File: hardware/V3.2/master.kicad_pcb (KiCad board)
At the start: 4 copper layers, 40 x 40 mm, 129 parts, among them J1 USB-C, J2 DRILL, J3 DRILL, J4 DRILL, J5 DRILL, J6 STACK-UP-HIGH, J7 STACK-HIGH, J8 STACK-UP-LOW, J9 STACK-DOWN, P1 Port A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

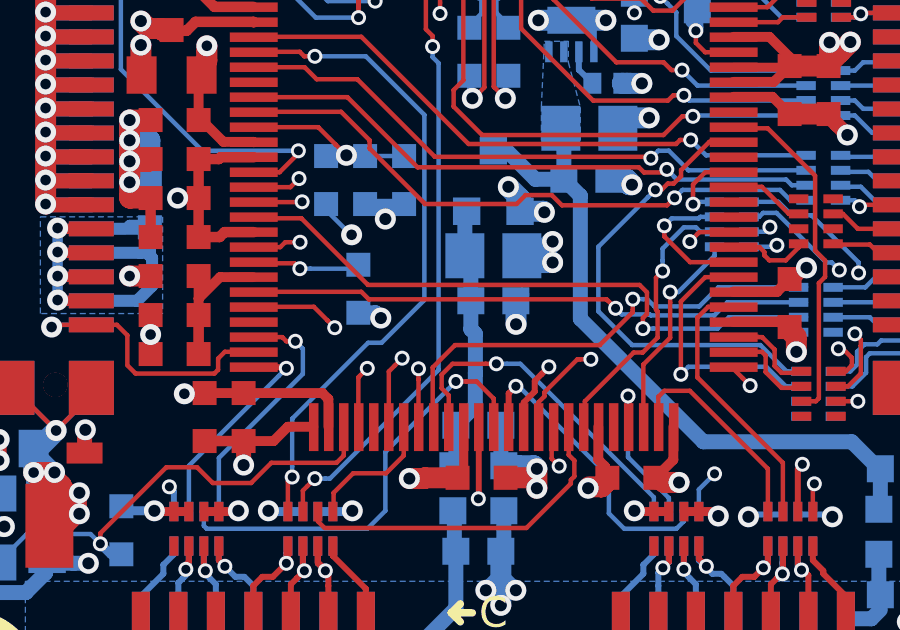
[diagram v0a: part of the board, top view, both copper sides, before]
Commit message: fix rts/rx pin swap, add version 3.2 pin detect
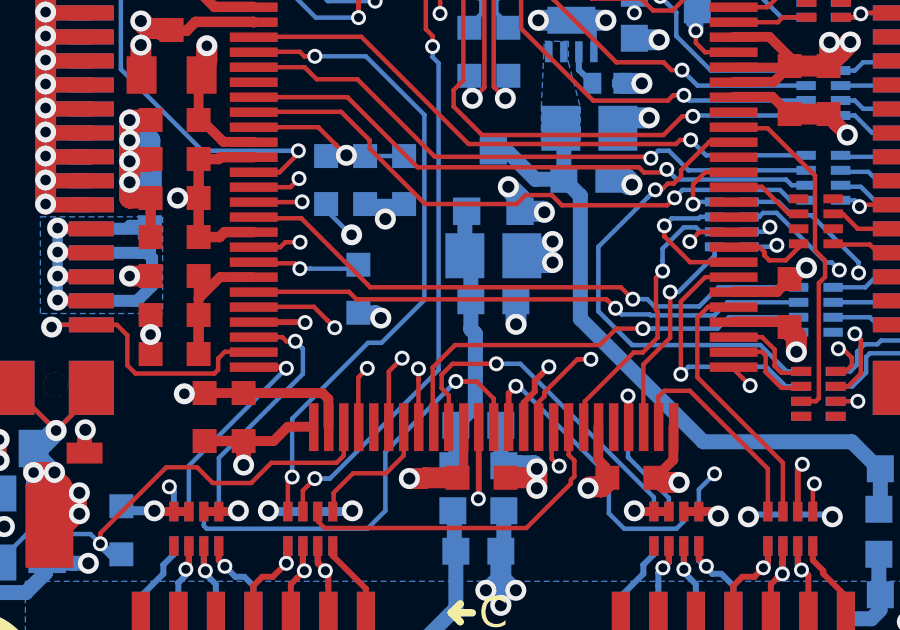
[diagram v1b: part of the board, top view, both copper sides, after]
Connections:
- RP304 pad 2: STACK-SER2-RXD -> STACK-SER2-RTS
- RP304 pad 4: STACK-SER2-RTS -> STACK-SER2-RXD
- RP307 pad 1: STACK-EX-0-GP00 -> STACK-EX-0-GP01
- RP307 pad 2: STACK-EX-0-GP01 -> STACK-EX-0-GP00
- U1 pad 22: Net-(U1-Pad22) -> GND
- U1 pad 44: STACK-EX-0-GP01 -> STACK-EX-0-GP00
- U1 pad 48: STACK-EX-0-GP00 -> STACK-EX-0-GP01
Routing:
- net STACK-EX-0-GP01: track 9.52 -> 7.09 mm
- net STACK-EX-0-GP00: track 7.09 -> 9.52 mm
- net GND: track 217.4 -> 219.1 mm, vias 82 -> 83
- net STACK-SER2-RXD: track 21.1 -> 20.0 mm
- net STACK-SER2-RTS: track 16.0 -> 15.2 mm
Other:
- board text added: "Copyright Tinkerforge GmbH 2022. This documentation describes Open Hardware and is licensed under the CERN OHL v. 1.1. You may redistribute and modify this documentation under the terms of the CERN OHL v.1.1. (http://ohwr.org/cernohl). This documentation is distributed WITHOUT ANY EXPRESS OR IMPLIED WARRANTY, INCLUDING OF MERCHANTABILITY, SATISFACTORY QUALITY AND FITNESS FOR A PARTICULAR PURPOSE.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"
- board text removed: "Copyright Tinkerforge GmbH 2020. This documentation describes Open Hardware and is licensed under the CERN OHL v. 1.1. You may redistribute and modify this documentation under the terms of the CERN OHL v.1.1. (http://ohwr.org/cernohl). This documentation is distributed WITHOUT ANY EXPRESS OR IMPLIED WARRANTY, INCLUDING OF MERCHANTABILITY, SATISFACTORY QUALITY AND FITNESS FOR A PARTICULAR PURPOSE.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"
